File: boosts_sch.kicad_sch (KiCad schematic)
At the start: 43 parts, among them IC1 AP2205-W5-7, IC2 AP2205-W5-7, IC3 TPS61089RNRR, IC4 TPS61089RNRR

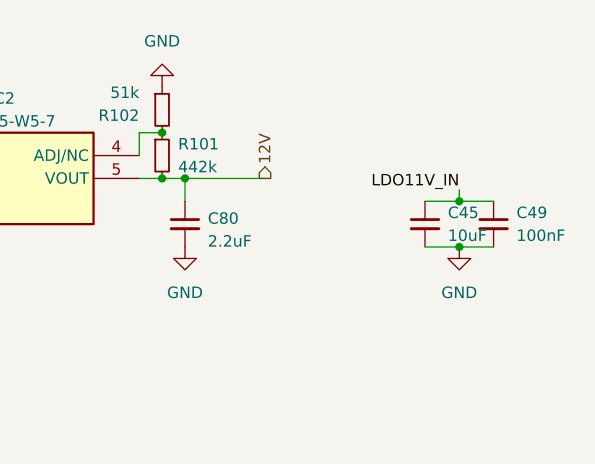
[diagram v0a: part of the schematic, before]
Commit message: Xavier: Modified ADS board
Pressure Sensor ADS board reduced to ADS131M03 with 3 channels for the 3 pressure sensors
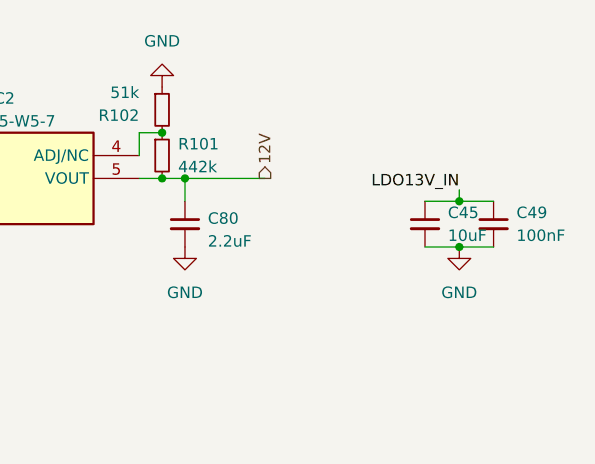
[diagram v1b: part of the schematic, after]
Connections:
- net LDO11V_IN is gone; now on net LDO13V_IN: C45.1, C49.1
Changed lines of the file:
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@@
     (effects (font (size 1.27 1.27)) (justify left bottom))
   )
-  (label "LDO11V_IN" (at 253.492 43.942 180) (fields_autoplaced)
+  (label "LDO13V_IN" (at 253.492 43.942 180) (fields_autoplaced)
     (effects (font (size 1.27 1.27)) (justify right bottom))
   )

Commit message: update
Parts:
- L4, L5: footprint iclr:SRR6038 -> iclr:IND_SRP6540-390M
- R101: value 442k -> 360k
- R65: value 976k -> 953k
- R99: value 100k -> 118k
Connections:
- net 12V renamed 10V
- net FB_12V renamed FB_10V
- net LDO13V_IN renamed LDO11V_IN
- net SW_12V renamed SW_10V
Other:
- note added: "Vout"

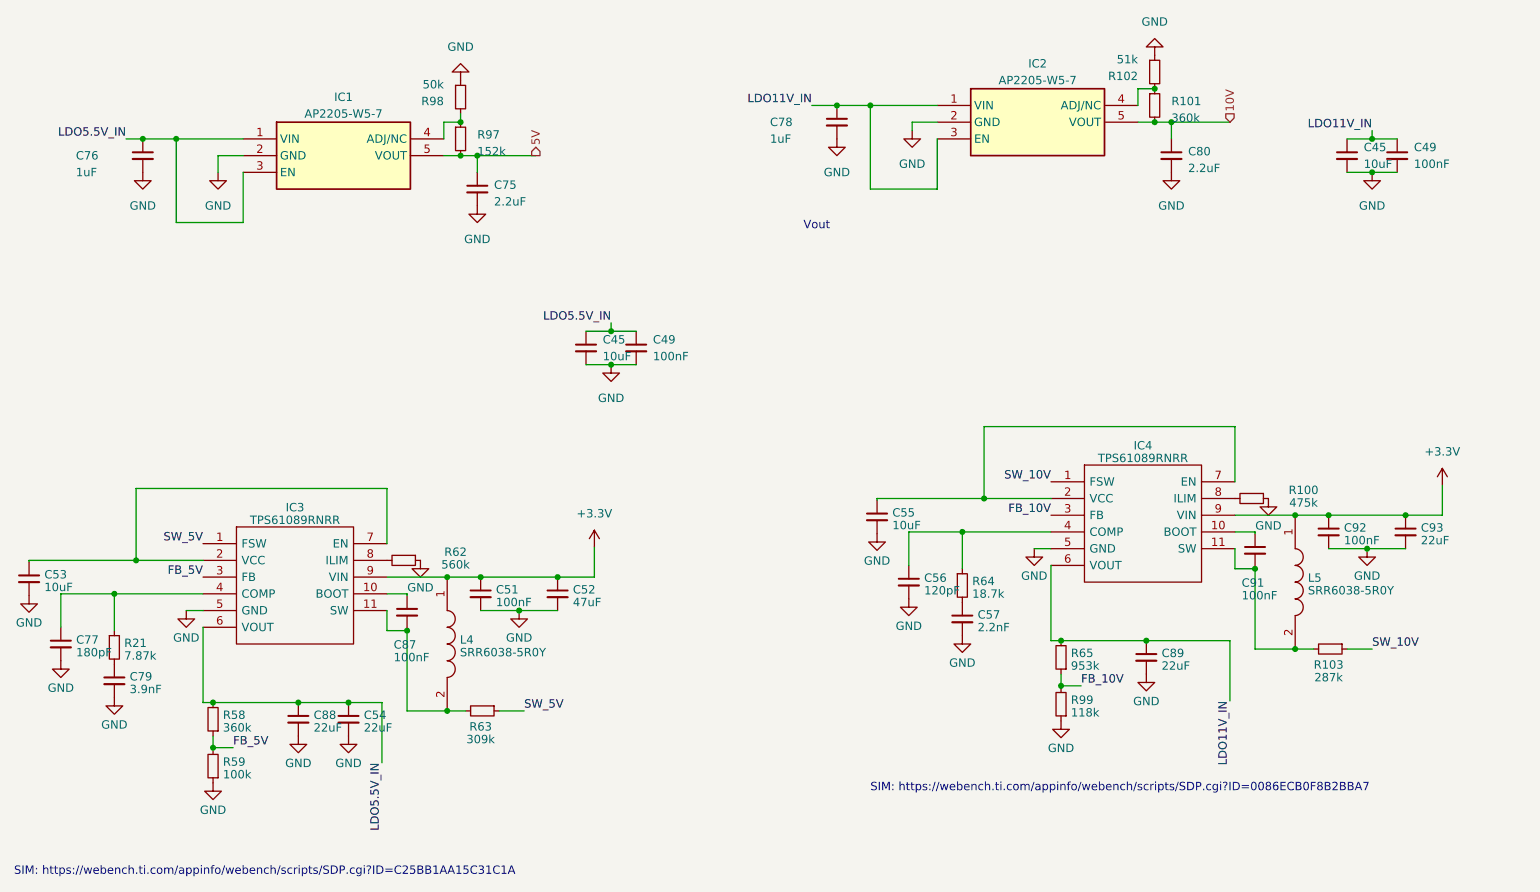
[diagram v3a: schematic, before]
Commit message: Schematic done, components layed out, sensors wired up
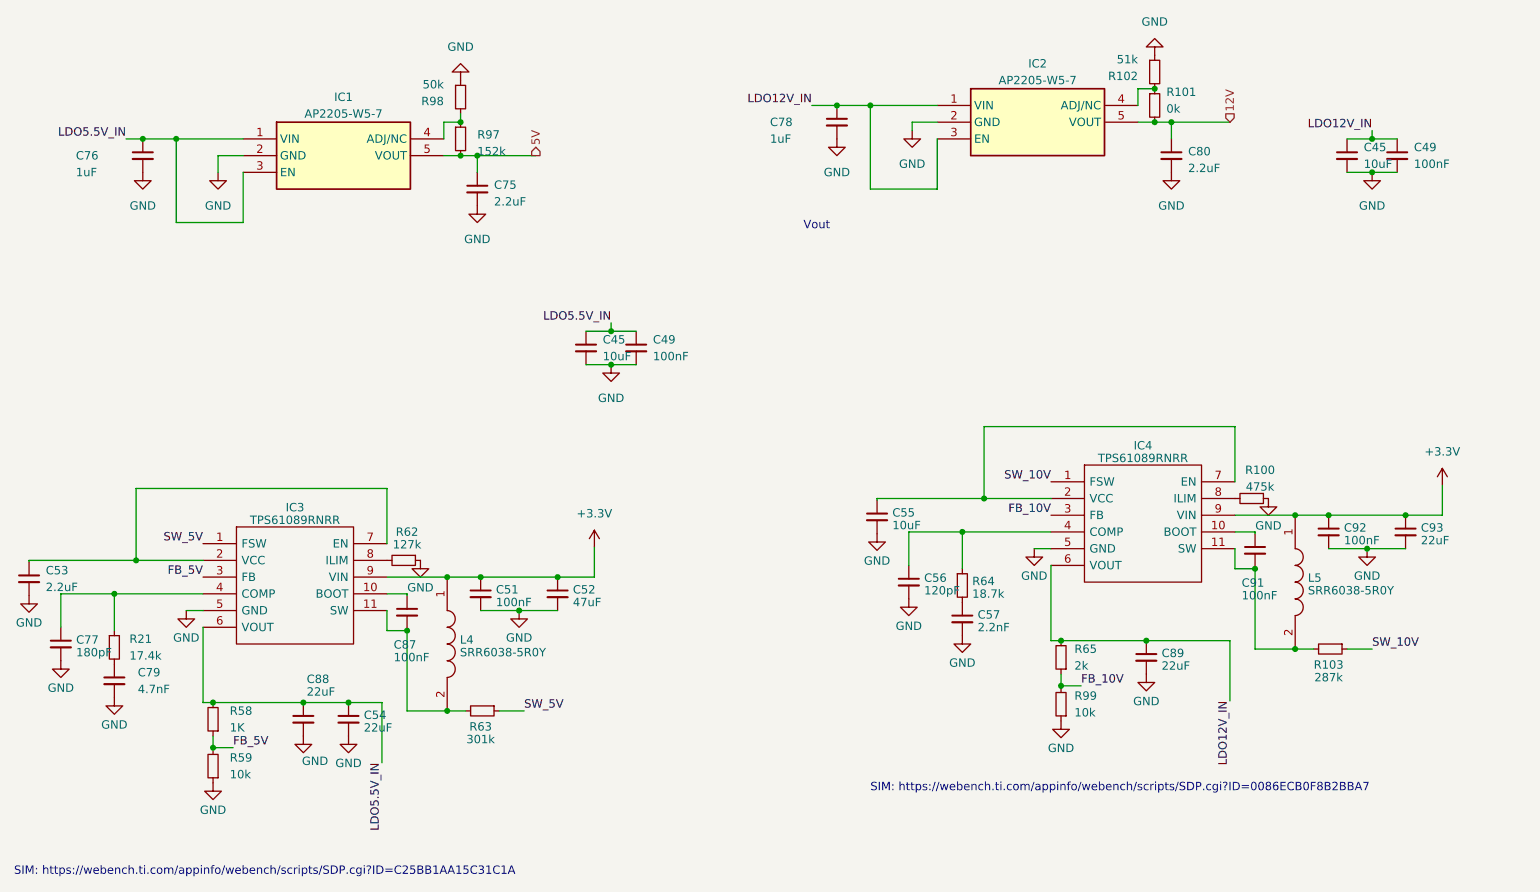
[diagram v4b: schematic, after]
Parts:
- C53: value 10uF -> 2.2uF
- C79: value 3.9nF -> 4.7nF
- R101: value 360k -> 0k
- R21: value 7.87k -> 17.4k
- R58: value 360k -> 1K
- R59: value 100k -> 10k
- R62: value 560k -> 127k
- R63: value 309k -> 301k
- R65: value 953k -> 2k
- R99: value 118k -> 10k
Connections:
- net 10V renamed 12V
- net LDO11V_IN renamed LDO12V_IN
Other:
- moved on the sheet: C88
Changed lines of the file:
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@@
   (junction (at 217.932 37.592) (diameter 0) (color 0 0 0 0)
   )
+  (junction (at 88.646 125.73) (diameter 0) (color 0 0 0 0)
+  )
   (junction (at 239.268 97.282) (diameter 0) (color 0 0 0 0)
   )
@@
   (junction (at 250.952 40.132) (diameter 0) (color 0 0 0 0)
   )
-  (junction (at 87.884 125.73) (diameter 0) (color 0 0 0 0)
-  )
   (junction (at 69.342 40.132) (diameter 0) (color 0 0 0 0)
   )
@@
     (stroke (width 0) (type default))
   )
+  (wire (pts (xy 74.93 125.73) (xy 88.646 125.73))
+    (stroke (width 0) (type default))
+  )
   (wire (pts (xy 202.184 116.332) (xy 203.708 116.332))
     (stroke (width 0) (type default))
@@
     (stroke (width 0) (type default))
   )
-  (wire (pts (xy 87.884 125.73) (xy 95.504 125.73))
-    (stroke (width 0) (type default))
-  )
   (wire (pts (xy 216.662 116.332) (xy 229.362 116.332))
     (stroke (width 0) (type default))
@@
     (stroke (width 0) (type default))
   )
+  (wire (pts (xy 88.646 125.73) (xy 95.504 125.73))
+    (stroke (width 0) (type default))
+  )
   (wire (pts (xy 184.912 37.592) (xy 181.102 37.592))
     (stroke (width 0) (type default))
@@
   )
   (wire (pts (xy 104.394 127) (xy 104.394 114.808))
-    (stroke (width 0) (type default))
-  )
-  (wire (pts (xy 74.93 125.73) (xy 87.884 125.73))
     (stroke (width 0) (type default))
   )
@@
     (effects (font (size 1.27 1.27)) (justify left bottom))
   )
-  (label "LDO11V_IN" (at 165.862 35.052 180) (fields_autoplaced)
+  (label "LDO12V_IN" (at 165.862 35.052 180) (fields_autoplaced)
     (effects (font (size 1.27 1.27)) (justify right bottom))
   )
@@
     (effects (font (size 1.27 1.27)) (justify right bottom))
   )
-  (label "LDO11V_IN" (at 229.362 125.476 270) (fields_autoplaced)
+  (label "LDO12V_IN" (at 229.362 125.476 270) (fields_autoplaced)
     (effects (font (size 1.27 1.27)) (justify right bottom))
   )
-  (label "LDO11V_IN" (at 250.952 38.862 180) (fields_autoplaced)
+  (label "LDO12V_IN" (at 250.952 38.862 180) (fields_autoplaced)
     (effects (font (size 1.27 1.27)) (justify right bottom))
   )
@@
     (effects (font (size 1.27 1.27)) (justify left))
   )
-  (hierarchical_label "10V" (shape input) (at 229.362 37.592 90) (fields_autoplaced)
+  (hierarchical_label "12V" (shape input) (at 229.362 37.592 90) (fields_autoplaced)
     (effects (font (size 1.27 1.27)) (justify left))
   )
@@
   (symbol (lib_id "Device:R_Small") (at 103.886 104.14 270) (unit 1)
     (in_bom yes) (on_board yes) (dnp no)
-    (property "Reference" "R62" (at 111.76 102.87 90)
-      (effects (font (size 1.27 1.27)))
-    )
-    (property "Value" "560k" (at 111.76 104.791 90)
+    (property "Reference" "R62" (at 104.394 99.822 90)
+      (effects (font (size 1.27 1.27)))
+    )
+    (property "Value" "127k" (at 104.394 101.743 90)
       (effects (font (size 1.27 1.27)))
     )
@@
     )
   )
-  (symbol (lib_name "GND_4") (lib_id "power:GND") (at 87.884 130.81 0) (unit 1)
-    (in_bom yes) (on_board yes) (dnp no) (fields_autoplaced)
-    (property "Reference" "#PWR0135" (at 87.884 137.16 0)
-      (effects (font (size 1.27 1.27)) hide)
-    )
-    (property "Value" "GND" (at 87.884 134.9455 0)
-      (effects (font (size 1.27 1.27)))
-    )
-    (property "Footprint" "" (at 87.884 130.81 0)
-      (effects (font (size 1.27 1.27)) hide)
-    )
-    (property "Datasheet" "" (at 87.884 130.81 0)
+  (symbol (lib_name "GND_4") (lib_id "power:GND") (at 88.646 130.81 0) (unit 1)
+    (in_bom yes) (on_board yes) (dnp no)
+    (property "Reference" "#PWR0135" (at 88.646 137.16 0)
+      (effects (font (size 1.27 1.27)) hide)
+    )
+    (property "Value" "GND" (at 90.424 134.62 0)
+      (effects (font (size 1.27 1.27)))
+    )
+    (property "Footprint" "" (at 88.646 130.81 0)
+      (effects (font (size 1.27 1.27)) hide)
+    )
+    (property "Datasheet" "" (at 88.646 130.81 0)
       (effects (font (size 1.27 1.27)) hide)
     )
@@
   (symbol (lib_id "Device:R_Small") (at 232.664 94.742 270) (unit 1)
     (in_bom yes) (on_board yes) (dnp no)
-    (property "Reference" "R100" (at 240.538 93.472 90)
-      (effects (font (size 1.27 1.27)))
-    )
-    (property "Value" "475k" (at 240.538 95.393 90)
+    (property "Reference" "R100" (at 233.934 90.424 90)
+      (effects (font (size 1.27 1.27)))
+    )
+    (property "Value" "475k" (at 233.934 92.964 90)
       (effects (font (size 1.27 1.27)))
     )
@@
   (symbol (lib_id "Device:C_Small") (at 59.944 122.428 0) (unit 1)
     (in_bom yes) (on_board yes) (dnp no) (fields_autoplaced)
-    (property "Reference" "C79" (at 62.2681 121.7906 0)
-      (effects (font (size 1.27 1.27)) (justify left))
-    )
-    (property "Value" "3.9nF" (at 62.2681 123.7116 0)
+    (property "Reference" "C79" (at 63.5 121.1643 0)
+      (effects (font (size 1.27 1.27)) (justify left))
+    )
+    (property "Value" "4.7nF" (at 63.5 123.7043 0)
       (effects (font (size 1.27 1.27)) (justify left))
     )
@@
     )
   )
-  (symbol (lib_id "Device:C_Small") (at 87.884 128.27 0) (unit 1)
-    (in_bom yes) (on_board yes) (dnp no) (fields_autoplaced)
-    (property "Reference" "C88" (at 90.2081 127.6326 0)
-      (effects (font (size 1.27 1.27)) (justify left))
-    )
-    (property "Value" "22uF" (at 90.2081 129.5536 0)
-      (effects (font (size 1.27 1.27)) (justify left))
-    )
-    (property "Footprint" "Capacitor_SMD:C_0805_2012Metric" (at 87.884 128.27 0)
-      (effects (font (size 1.27 1.27)) hide)
-    )
-    (property "Datasheet" "~" (at 87.884 128.27 0)
+  (symbol (lib_id "Device:C_Small") (at 88.646 128.27 0) (unit 1)
+    (in_bom yes) (on_board yes) (dnp no)
+    (property "Reference" "C88" (at 89.154 122.174 0)
+      (effects (font (size 1.27 1.27)) (justify left))
+    )
+    (property "Value" "22uF" (at 89.154 124.095 0)
+      (effects (font (size 1.27 1.27)) (justify left))
+    )
+    (property "Footprint" "Capacitor_SMD:C_0805_2012Metric" (at 88.646 128.27 0)
+      (effects (font (size 1.27 1.27)) hide)
+    )
+    (property "Datasheet" "~" (at 88.646 128.27 0)
       (effects (font (size 1.27 1.27)) hide)
     )
@@
   (symbol (lib_id "Device:R_Small") (at 203.708 118.872 180) (unit 1)
     (in_bom yes) (on_board yes) (dnp no) (fields_autoplaced)
-    (property "Reference" "R65" (at 205.2066 118.2283 0)
+    (property "Reference" "R65" (at 205.74 117.602 0)
       (effects (font (size 1.27 1.27)) (justify right))
     )
-    (property "Value" "953k" (at 205.2066 120.1493 0)
+    (property "Value" "2k" (at 205.74 120.142 0)
       (effects (font (size 1.27 1.27)) (justify right))
     )
@@
   (symbol (lib_id "Device:R_Small") (at 203.708 125.984 180) (unit 1)
     (in_bom yes) (on_board yes) (dnp no) (fields_autoplaced)
-    (property "Reference" "R99" (at 205.2066 125.3403 0)
+    (property "Reference" "R99" (at 205.74 124.714 0)
       (effects (font (size 1.27 1.27)) (justify right))
     )
-    (property "Value" "118k" (at 205.2066 127.2613 0)
+    (property "Value" "10k" (at 205.74 127.254 0)
       (effects (font (size 1.27 1.27)) (justify right))
     )
@@
   (symbol (lib_id "Device:R_Small") (at 59.944 117.348 0) (unit 1)
     (in_bom yes) (on_board yes) (dnp no) (fields_autoplaced)
-    (property "Reference" "R21" (at 61.4426 116.7043 0)
-      (effects (font (size 1.27 1.27)) (justify left))
-    )
-    (property "Value" "7.87k" (at 61.4426 118.6253 0)
+    (property "Reference" "R21" (at 62.23 116.078 0)
+      (effects (font (size 1.27 1.27)) (justify left))
+    )
+    (property "Value" "17.4k" (at 62.23 118.618 0)
       (effects (font (size 1.27 1.27)) (justify left))
     )
@@
   (symbol (lib_id "Device:R_Small") (at 74.93 128.27 180) (unit 1)
     (in_bom yes) (on_board yes) (dnp no) (fields_autoplaced)
-    (property "Reference" "R58" (at 76.4286 127.6263 0)
+    (property "Reference" "R58" (at 77.47 127 0)
       (effects (font (size 1.27 1.27)) (justify right))
     )
-    (property "Value" "360k" (at 76.4286 129.5473 0)
+    (property "Value" "1K" (at 77.47 129.54 0)
       (effects (font (size 1.27 1.27)) (justify right))
     )
@@
   (symbol (lib_id "Device:C_Small") (at 46.99 106.934 0) (unit 1)
     (in_bom yes) (on_board yes) (dnp no) (fields_autoplaced)
-    (property "Reference" "C53" (at 49.3141 106.2966 0)
-      (effects (font (size 1.27 1.27)) (justify left))
-    )
-    (property "Value" "10uF" (at 49.3141 108.2176 0)
+    (property "Reference" "C53" (at 49.53 105.6703 0)
+      (effects (font (size 1.27 1.27)) (justify left))
+    )
+    (property "Value" "2.2uF" (at 49.53 108.2103 0)
       (effects (font (size 1.27 1.27)) (justify left))
     )
@@
   )
   (symbol (lib_id "Device:R_Small") (at 217.932 35.052 0) (unit 1)
-    (in_bom yes) (on_board yes) (dnp no) (fields_autoplaced)
-    (property "Reference" "R101" (at 220.472 34.417 0)
-      (effects (font (size 1.27 1.27)) (justify left))
-    )
-    (property "Value" "360k" (at 220.472 36.957 0)
+    (in_bom yes) (on_board yes) (dnp no)
+    (property "Reference" "R101" (at 219.71 33.02 0)
+      (effects (font (size 1.27 1.27)) (justify left))
+    )
+    (property "Value" "0k" (at 219.71 35.56 0)
       (effects (font (size 1.27 1.27)) (justify left))
     )
@@
   (symbol (lib_id "Device:R_Small") (at 74.93 135.382 180) (unit 1)
     (in_bom yes) (on_board yes) (dnp no) (fields_autoplaced)
-    (property "Reference" "R59" (at 76.4286 134.7383 0)
+    (property "Reference" "R59" (at 77.47 134.112 0)
       (effects (font (size 1.27 1.27)) (justify right))
     )
-    (property "Value" "100k" (at 76.4286 136.6593 0)
+    (property "Value" "10k" (at 77.47 136.652 0)
       (effects (font (size 1.27 1.27)) (justify right))
     )
@@
       (effects (font (size 1.27 1.27)))
     )
-    (property "Value" "309k" (at 115.57 131.318 90)
-      (effects (font (size 1.27 1.27)))
-    )
+    (property "Value" "301k" (at 115.57 131.318 90)
+      (effects (font (size 1.27 1.27)))
+    )

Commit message: Most Review 1 changes made
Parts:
- removed R101: 0k, Resistor_SMD:R_0402_1005Metric, symbol Device:R_Small
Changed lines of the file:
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@@
   (junction (at 110.49 127) (diameter 0) (color 0 0 0 0)
   )
-  (junction (at 217.932 37.592) (diameter 0) (color 0 0 0 0)
-  )
   (junction (at 88.646 125.73) (diameter 0) (color 0 0 0 0)
   )
@@
   (junction (at 59.944 109.22) (diameter 0) (color 0 0 0 0)
   )
-  (junction (at 217.932 32.512) (diameter 0) (color 0 0 0 0)
-  )
   (junction (at 112.522 37.592) (diameter 0) (color 0 0 0 0)
   )
@@
     (stroke (width 0) (type default))
   )
-  (wire (pts (xy 220.472 37.592) (xy 217.932 37.592))
-    (stroke (width 0) (type default))
-  )
   (wire (pts (xy 250.19 102.362) (xy 256.032 102.362))
     (stroke (width 0) (type default))
@@
     (stroke (width 0) (type default))
   )
-  (wire (pts (xy 217.932 37.592) (xy 215.392 37.592))
+  (wire (pts (xy 215.392 37.592) (xy 220.472 37.592))
     (stroke (width 0) (type default))
   )
@@
         )
       )
-    )
-  )
-  (symbol (lib_id "Device:R_Small") (at 217.932 35.052 0) (unit 1)
-    (in_bom yes) (on_board yes) (dnp no)
-    (property "Reference" "R101" (at 219.71 33.02 0)
-      (effects (font (size 1.27 1.27)) (justify left))
-    )
-    (property "Value" "0k" (at 219.71 35.56 0)
-      (effects (font (size 1.27 1.27)) (justify left))
-    )
-    (property "Footprint" "Resistor_SMD:R_0402_1005Metric" (at 217.932 35.052 0)
-      (effects (font (size 1.27 1.27)) hide)
-    )
-    (property "Datasheet" "~" (at 217.932 35.052 0)
-      (effects (font (size 1.27 1.27)) hide)
-    )
-    (pin "1")
-    (pin "2")
-    (instances
-      (project "sensorboard"
-        (path "/26801cfb-b53b-4a6a-a2f4-5f4986565765/de0f76c4-1b74-4c96-9fad-1f7da693b4f2"
-          (reference "R101") (unit 1)
-        )
-      )
-      (project "Ricardo-Stark"
-        (path "/7db990e4-92e1-4f99-b4d2-435bbec1ba83/df24f951-9014-423f-941d-dec7c0c4c8db"
-          (reference "R71") (unit 1)
-        )
-      )
-      (project "Boosts (1)"
-        (path "/b6157239-5ec1-4dd1-8800-2610bd2c0507"
-          (reference "R101") (unit 1)
-        )
-      )

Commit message: Review 1 Changes Complete
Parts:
- C79: value 4.7nF -> 3.9nF
- R21: value 17.4k -> 7.87k
- R58: value 1K -> 360k
- R59, R99: value 10k -> 100k
- R62: value 127k -> 560k
- R65: value 2k -> 900k
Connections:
- net FB_10V renamed FB_12V
- net SW_10V renamed SW_12V
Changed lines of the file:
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@@
     (effects (font (size 1.27 1.27)) (justify right bottom))
   )
-  (label "SW_10V" (at 250.952 117.602 0) (fields_autoplaced)
+  (label "SW_12V" (at 250.952 117.602 0) (fields_autoplaced)
     (effects (font (size 1.27 1.27)) (justify left bottom))
   )
@@
     (effects (font (size 1.27 1.27)) (justify right bottom))
   )
-  (label "SW_10V" (at 202.184 92.202 180) (fields_autoplaced)
+  (label "SW_12V" (at 202.184 92.202 180) (fields_autoplaced)
     (effects (font (size 1.27 1.27)) (justify right bottom))
   )
-  (label "FB_10V" (at 202.184 97.282 180) (fields_autoplaced)
+  (label "FB_12V" (at 202.184 97.282 180) (fields_autoplaced)
     (effects (font (size 1.27 1.27)) (justify right bottom))
   )
-  (label "FB_10V" (at 206.756 123.19 0) (fields_autoplaced)
+  (label "FB_12V" (at 206.756 123.19 0) (fields_autoplaced)
     (effects (font (size 1.27 1.27)) (justify left bottom))
   )
@@
       (effects (font (size 1.27 1.27)))
     )
-    (property "Value" "127k" (at 104.394 101.743 90)
+    (property "Value" "560k" (at 104.394 101.743 90)
       (effects (font (size 1.27 1.27)))
     )
@@
       (effects (font (size 1.27 1.27)) (justify left))
     )
-    (property "Value" "4.7nF" (at 63.5 123.7043 0)
+    (property "Value" "3.9nF" (at 63.5 123.7043 0)
       (effects (font (size 1.27 1.27)) (justify left))
     )
@@
       (effects (font (size 1.27 1.27)) (justify right))
     )
-    (property "Value" "2k" (at 205.74 120.142 0)
+    (property "Value" "900k" (at 205.74 120.142 0)
       (effects (font (size 1.27 1.27)) (justify right))
     )
@@
       (effects (font (size 1.27 1.27)) (justify right))
     )
-    (property "Value" "10k" (at 205.74 127.254 0)
+    (property "Value" "100k" (at 205.74 127.254 0)
       (effects (font (size 1.27 1.27)) (justify right))
     )
@@
       (effects (font (size 1.27 1.27)) (justify left))
     )
-    (property "Value" "17.4k" (at 62.23 118.618 0)
+    (property "Value" "7.87k" (at 62.23 118.618 0)
       (effects (font (size 1.27 1.27)) (justify left))
     )
@@
       (effects (font (size 1.27 1.27)) (justify right))
     )
-    (property "Value" "1K" (at 77.47 129.54 0)
+    (property "Value" "360k" (at 77.47 129.54 0)
       (effects (font (size 1.27 1.27)) (justify right))
     )
@@
       (effects (font (size 1.27 1.27)) (justify right))
     )
-    (property "Value" "10k" (at 77.47 136.652 0)
+    (property "Value" "100k" (at 77.47 136.652 0)
       (effects (font (size 1.27 1.27)) (justify right))
     )
